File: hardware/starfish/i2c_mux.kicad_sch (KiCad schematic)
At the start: 17 parts

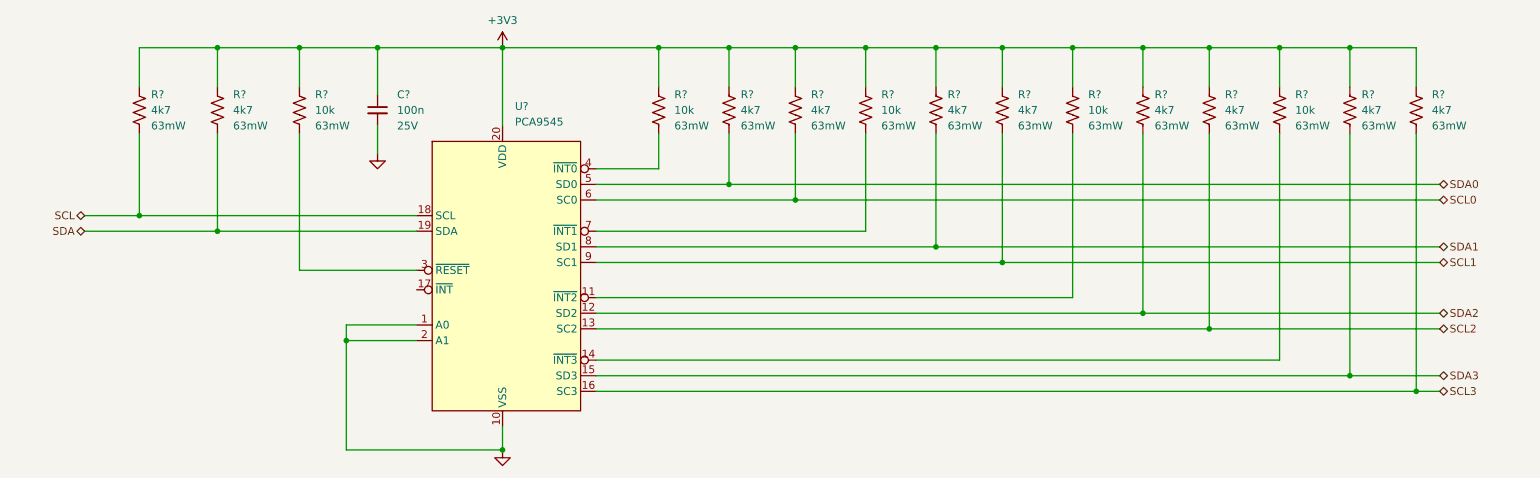
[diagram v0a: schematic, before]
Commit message: Mostly finished starfish schematic, ready for layout!
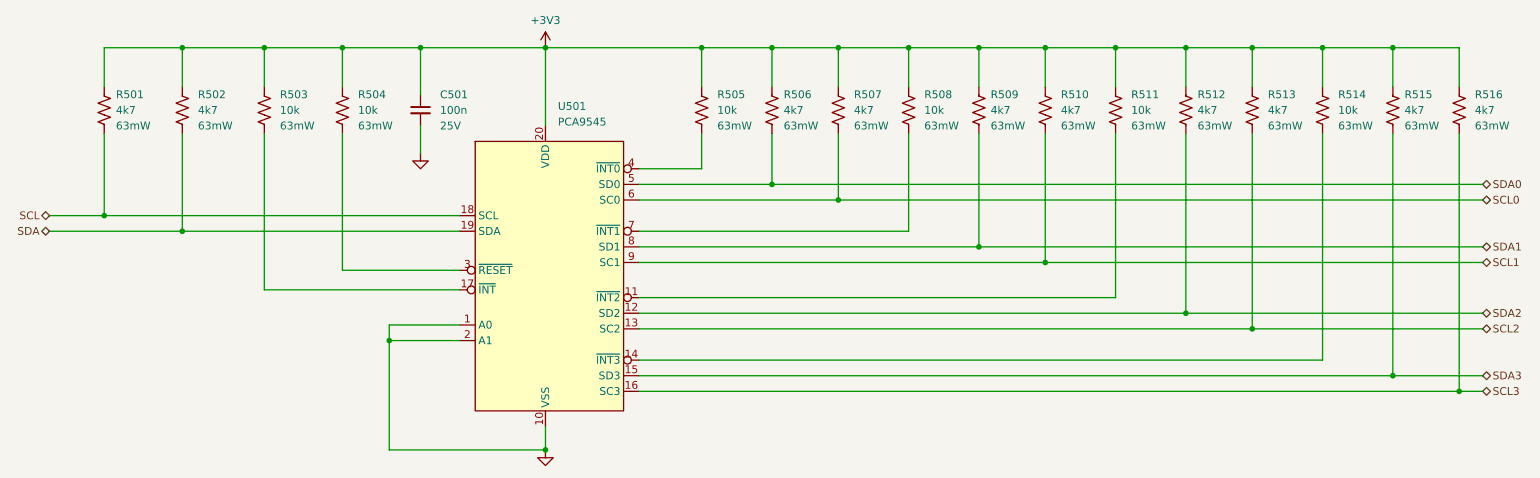
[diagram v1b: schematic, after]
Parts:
- added R504: 10k, winterbloom:R_0402_HandSolder, symbol Device:R_US
- C501: renamed from C?; footprint Capacitor_SMD:C_0402_1005Metric_Pad0.74x0.62mm_HandSolder -> winterbloom:C_0402_HandSolder
- R501, R502, R506, R507, R509, R510, R512, R513, R515, R516: renamed from R?; footprint (none) -> winterbloom:R_0402_HandSolder
- R503, R505, R508, R511, R514: renamed from R?; footprint (none) -> winterbloom:R_0402_HandSolder; mpn (none) -> RC0402JR-0710KL
- gave numbers to parts that had none: 1
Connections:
- net +3V3: now also R504.1
- net at U501.17 (~{INT}): now also R503.2
- net at U501.3 (~{RESET}): now also R504.2; no longer R503.2
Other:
- moved on the sheet: C501, R501, R502, R503, R505, R506, R507, R508, R509, R510, R511, R512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

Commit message: First pass at layout and routing
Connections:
- net ~{RESET}: now reaches R504.2, U501.3 (~{RESET})
- net ~{INT3}: now reaches R514.2, U501.14 (~{INT3})
- net ~{INT2}: now reaches R511.2, U501.11 (~{INT2})
- net INT: now reaches R503.2, U501.17 (~{INT})
- net ~{INT0}: now reaches R505.2, U501.4 (~{INT0})
- net ~{INT1}: now reaches R508.2, U501.7 (~{INT1})
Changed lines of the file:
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@@
     (stroke (width 0) (type default) (color 0 0 0 0))
+  )
+  (label "~{RESET}" (at 87.63 113.665 180)
+    (effects (font (size 0.64 0.64)) (justify right bottom))
+  )
+  (label "~{INT2}" (at 116.84 118.11 0)
+    (effects (font (size 0.64 0.64)) (justify left bottom))
+  )
+  (label "~{INT3}" (at 117.2422 128.27 0)
+    (effects (font (size 0.64 0.64)) (justify left bottom))
+  )
+  (label "~{INT0}" (at 116.84 97.155 0)
+    (effects (font (size 0.64 0.64)) (justify left bottom))
+  )
+  (label "INT" (at 87.63 116.84 180)
+    (effects (font (size 0.64 0.64)) (justify right bottom))
+  )
+  (label "~{INT1}" (at 116.84 107.315 0)
+    (effects (font (size 0.64 0.64)) (justify left bottom))
   )
   (hierarchical_label "SCL2" (shape bidirectional) (at 254 123.19 0)

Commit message: Run through purchasing, update some cap sizes
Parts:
- R501, R502, R506, R507, R509, R510, R512, R513, R515, R516: mpn (none) -> CRGCQ0402J4K7
- U501: mpn PCA9545APW,118 -> PCA9545APW, PCA9545BPW, PCA9545CPW
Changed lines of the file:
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@@
       (effects (font (size 1.27 1.27)) (justify left))
+    )
+    (property "mpn" "CRGCQ0402J4K7" (id 5) (at 239.395 87.63 0)
+      (effects (font (size 1.27 1.27)) hide)
     )
     (pin "1")
@@
       (effects (font (size 1.27 1.27)) (justify left))
     )
+    (property "mpn" "CRGCQ0402J4K7" (id 5) (at 42.545 87.63 0)
+      (effects (font (size 1.27 1.27)) hide)
+    )
     (pin "1")
     (pin "2")
@@
       (effects (font (size 1.27 1.27)) (justify left))
     )
+    (property "mpn" "CRGCQ0402J4K7" (id 5) (at 138.43 87.63 0)
+      (effects (font (size 1.27 1.27)) hide)
+    )
     (pin "1")
     (pin "2")
@@
       (effects (font (size 1.27 1.27)) (justify left))
     )
+    (property "mpn" "CRGCQ0402J4K7" (id 5) (at 149.225 87.63 0)
+      (effects (font (size 1.27 1.27)) hide)
+    )
     (pin "1")
     (pin "2")
@@
       (effects (font (size 1.27 1.27)) hide)
     )
-    (property "mpn" "PCA9545APW,118" (id 4) (at 103.6194 90.17 0)
+    (property "mpn" "PCA9545APW, PCA9545BPW, PCA9545CPW" (id 4) (at 103.6194 90.17 0)
       (effects (font (size 1.27 1.27)) (justify left) hide)
     )
@@
       (effects (font (size 1.27 1.27)) (justify left))
     )
+    (property "mpn" "CRGCQ0402J4K7" (id 5) (at 216.535 87.63 0)
+      (effects (font (size 1.27 1.27)) hide)
+    )
     (pin "1")
     (pin "2")
@@
       (effects (font (size 1.27 1.27)) (justify left))
     )
+    (property "mpn" "CRGCQ0402J4K7" (id 5) (at 172.085 87.63 0)
+      (effects (font (size 1.27 1.27)) hide)
+    )
     (pin "1")
     (pin "2")
@@
     (property "Rating" "63mW" (id 4) (at 185.42 90.1699 0)
       (effects (font (size 1.27 1.27)) (justify left))
+    )
+    (property "mpn" "CRGCQ0402J4K7" (id 5) (at 182.88 87.63 0)
+      (effects (font (size 1.27 1.27)) hide)
     )
     (pin "1")
@@
       (effects (font (size 1.27 1.27)) (justify left))
     )
+    (property "mpn" "CRGCQ0402J4K7" (id 5) (at 29.845 87.63 0)
+      (effects (font (size 1.27 1.27)) hide)
+    )
     (pin "1")
     (pin "2")
@@
       (effects (font (size 1.27 1.27)) (justify left))
     )
+    (property "mpn" "CRGCQ0402J4K7" (id 5) (at 250.19 87.63 0)
+      (effects (font (size 1.27 1.27)) hide)
+    )
     (pin "1")
     (pin "2")
@@
       (effects (font (size 1.27 1.27)) (justify left))
     )
-    (pin "1")
+    (property "mpn" "CRGCQ0402J4K7" (id 5) (at 205.74 87.63 0)
+      (effects (font (size 1.27 1.27)) hide)
+    )
+    (pin "1")
